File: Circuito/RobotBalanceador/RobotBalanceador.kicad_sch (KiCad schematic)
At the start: 57 parts, among them J1 Conn_01x04_Pin, J2 USB_B_Micro, J3 Barrel_Jack_Switch, J4 ENCODER, J5 ENCODER, J6 MOT 1, J7 MOT 2, SW1 SW_SPDT, U1 STM32F103C8Tx, U2 LMR62014XMF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

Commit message: Referencias y textos ajustados
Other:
- note added: "4) DRV8870 Datasheet"
- note removed: "4) L293D Shield"
- note removed: "4) L293x Ti"
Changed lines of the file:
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@@
 		)
 	)
-	(text "4) L293D Shield"
-		(exclude_from_sim no)
-		(at 12.446 182.626 0)
-		(effects
-			(font
-				(size 1.27 1.27)
-			)
-			(justify left bottom)
-			(href "http://wiki.sunfounder.cc/index.php?title=L293D_Motor_Driver_Shield")
+	(text "4) DRV8870 Datasheet"
+		(exclude_from_sim no)
+		(at 12.446 180.086 0)
+		(effects
+			(font
+				(size 1.27 1.27)
+			)
+			(justify left bottom)
+			(href "https://www.ti.com/lit/ds/symlink/drv8870.pdf")
 		)
 	)
@@
 	(text "5) MPU6050 Adafruit"
 		(exclude_from_sim no)
-		(at 12.446 186.436 0)
+		(at 12.446 183.642 0)
 		(effects
 			(font
@@
 		)
 	)
-	(text "4) L293x Ti"
-		(exclude_from_sim no)
-		(at 12.446 173.736 0)
-		(effects
-			(font
-				(size 1.27 1.27)
-			)
-			(justify left bottom)
-			(href "https://www.ti.com/lit/ds/symlink/l293.pdf")
-		)
-	)
 	(text "*C) Puede que no sea necesario el switch mejor\nquitar para reducir componentes"
 		(exclude_from_sim no)
@@
 	(text "6) Video de Phil 30:50"
 		(exclude_from_sim no)
-		(at 12.446 190.246 0)
-		(effects
-			(font
+		(at 12.446 187.452 0)
+		(effects
+			(font

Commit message: Secciones ajustadas
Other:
- note added: "2) Conv. Boost 3.7 ~ 5V & 12V"
- note added: "3) Regulación"
- note added: "4) Motores"
- note added: "5) IMU"
- note added: "7) Encoder"
- note removed: "2) Conv. Boost 3.7 LIPO a 12V (LMR62014)"
- note removed: "3) Regulación 5V a 3.3V"
- note removed: "4) Puente H (DRV8870DDA)"
- note removed: "5) IMU (MPU6050)"
- note removed: "6) Conector p/ encoder"
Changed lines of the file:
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@@
 		)
 	)
-	(text "6) Conector p/\nencoder\n"
+	(text "7) Encoder"
 		(exclude_from_sim no)
-		(at 245.11 123.19 0)
+		(at 244.602 118.872 0)
 		(effects
 			(font
@@
 		)
 	)
-	(text "3) Regulación 5V a 3.3V"
+	(text "3) Regulación"
 		(exclude_from_sim no)
-		(at 207.772 19.304 0)
+		(at 207.518 18.542 0)
 		(effects
 			(font
@@
 		)
 	)
-	(text "4) Puente H (DRV8870DDA)"
+	(text "4) Motores"
 		(exclude_from_sim no)
 		(at 115.062 106.426 0)
@@
 		)
 	)
-	(text "2) Conv. Boost 3.7 LIPO a 12V\n(LMR62014)"
+	(text "2) Conv. Boost 3.7 ~ 5V & 12V"
 		(exclude_from_sim no)
-		(at 115.062 22.86 0)
+		(at 115.062 19.05 0)
 		(effects
 			(font
@@
 		)
 	)
-	(text "5) IMU (MPU6050)"
+	(text "5) IMU"
 		(exclude_from_sim no)
 		(at 207.772 56.896 0)

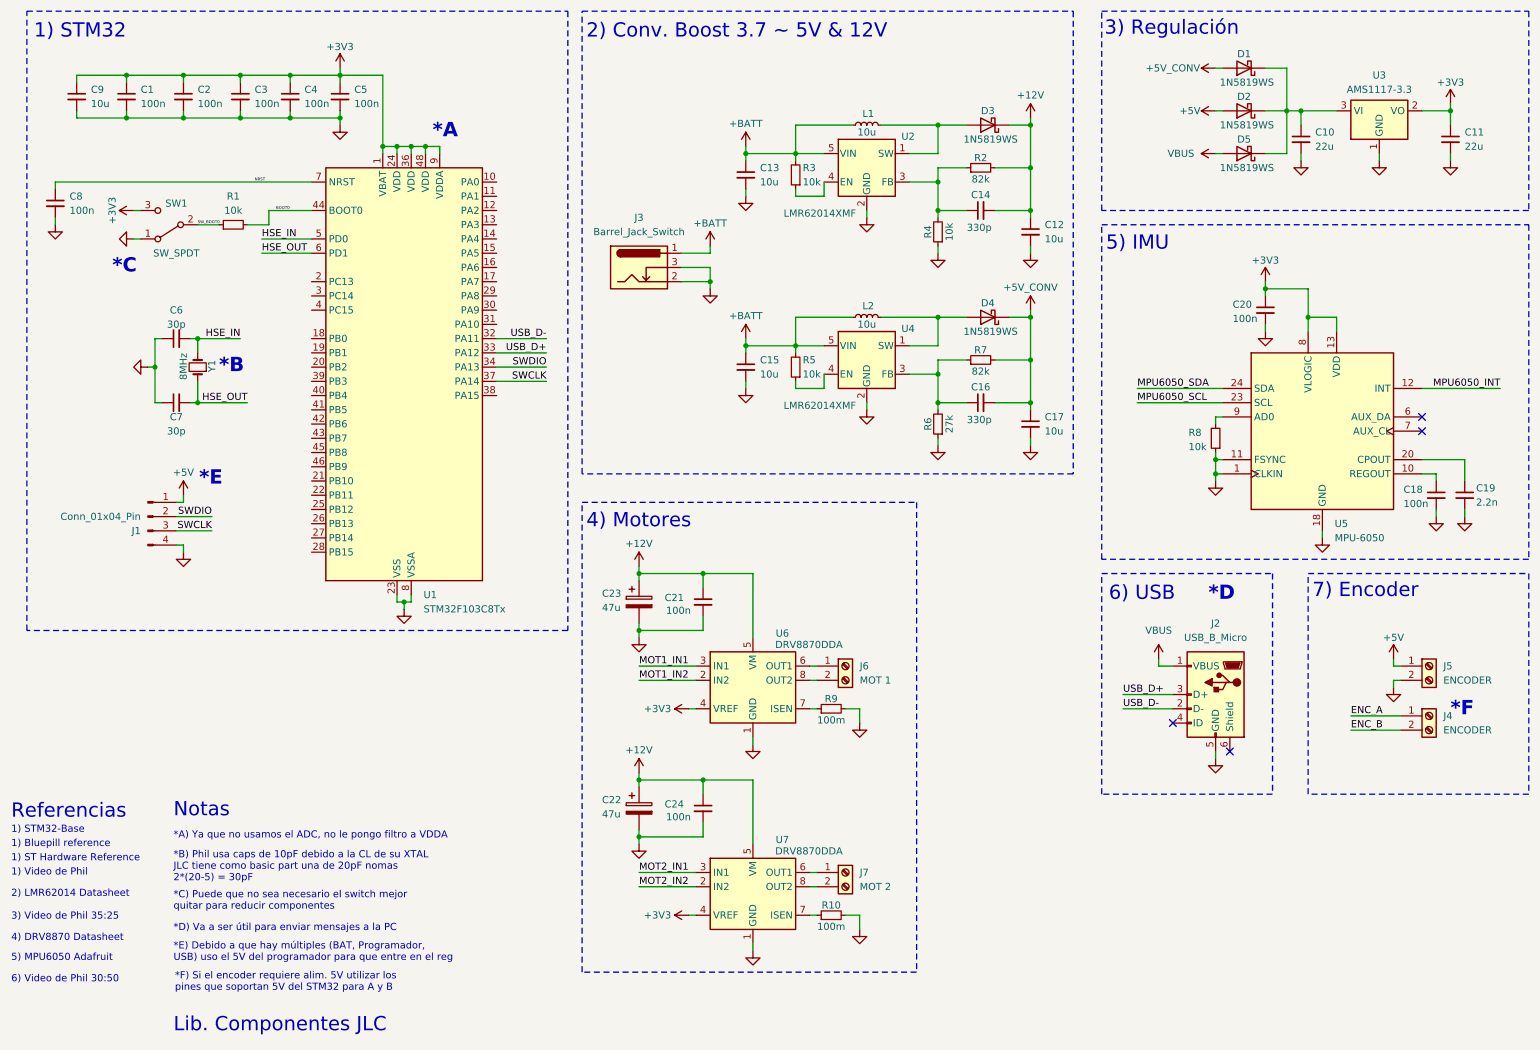
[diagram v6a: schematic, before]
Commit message: Añadido código/configuraciones para IMU y Encoder
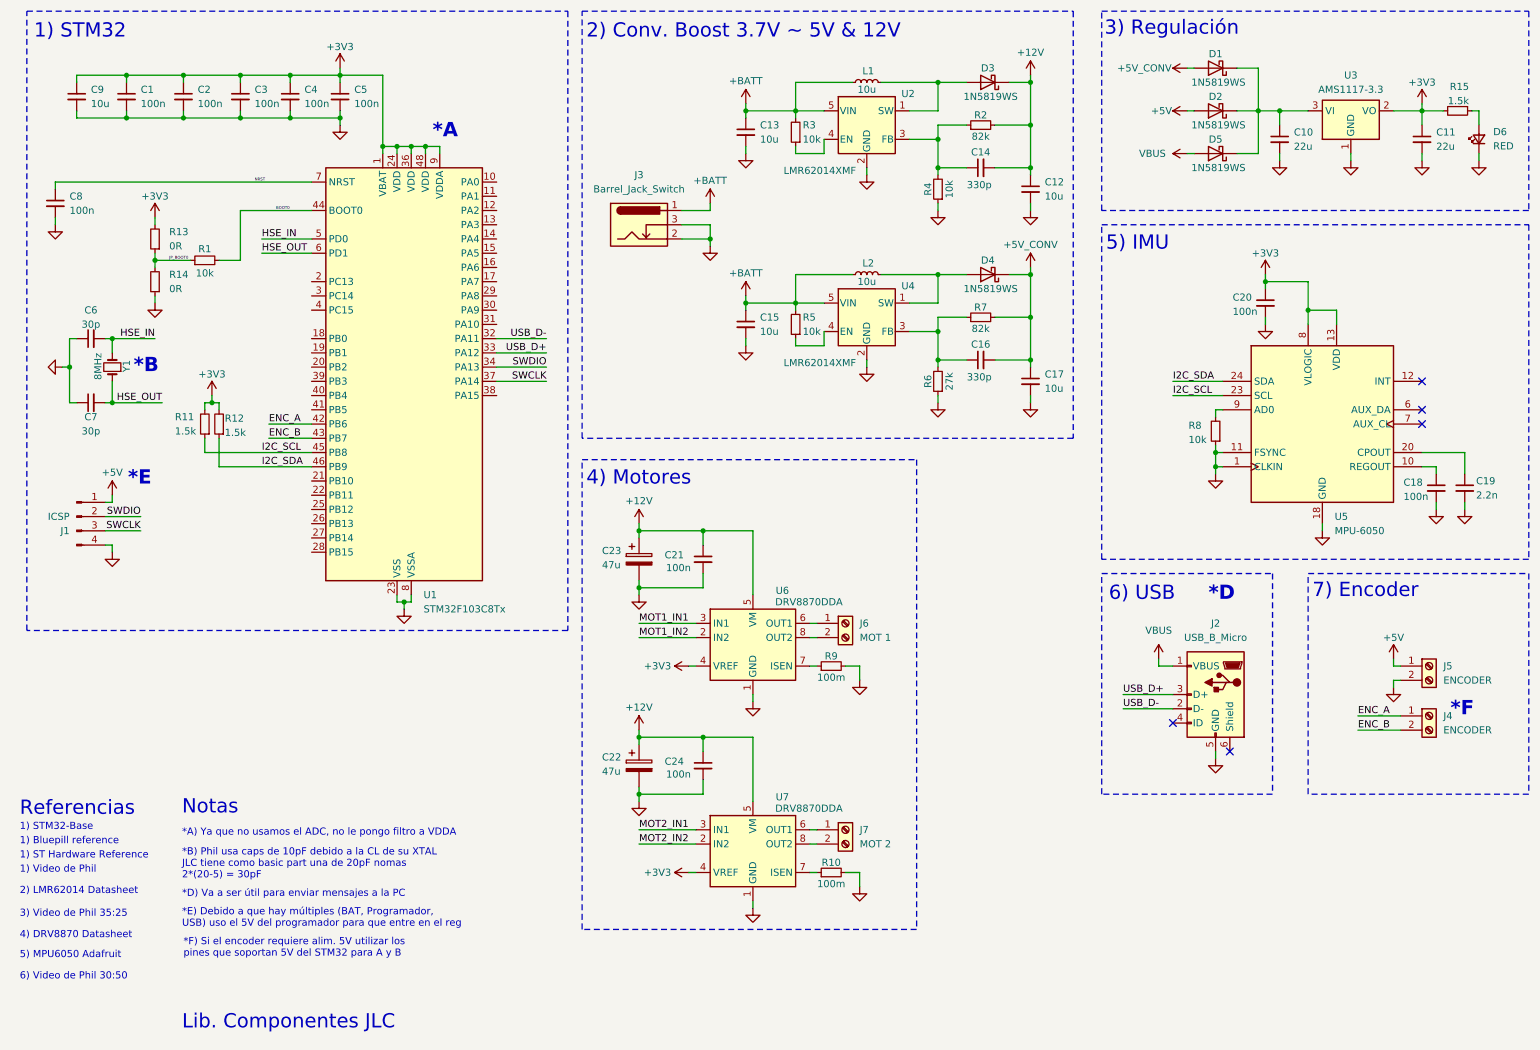
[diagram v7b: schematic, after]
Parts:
- removed SW1: SW_SPDT, symbol Switch:SW_SPDT
- added D6: RED, LED_SMD:LED_0603_1608Metric, symbol Device:LED_Small
- added R11, R12, R15: 1.5k, Resistor_SMD:R_0603_1608Metric, symbol Device:R_Small
- added R13, R14: 0R, Resistor_SMD:R_0402_1005Metric, symbol Device:R_Small
- J1: value Conn_01x04_Pin -> ICSP
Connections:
- net MPU6050_SCL is gone; now on net I2C_SCL: U5.23 (SCL)
- net MPU6050_SDA is gone; now on net I2C_SDA: U5.24 (SDA)
- net +3V3: now also R11.2, R12.2, R13.2, R15.2
- net ENC_A: now also U1.42 (PB6)
- net ENC_B: now also U1.43 (PB7)
- net GND: now also D6.1 (K), R14.1
- net I2C_SCL: now reaches U1.45 (PB8)
- net I2C_SCL: now also R11.1
- net I2C_SDA: now reaches U1.46 (PB9)
- net I2C_SDA: now also R12.1
- net MPU6050_INT: no longer names the net of U5.12 (INT)
- net SW_BOOT0 renamed JP_BOOT0
- net JP_BOOT0: now also R13.1, R14.2
- new net: D6.2 (A), R15.1
- no-connect marks 4 -> 5
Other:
- note added: "2) Conv. Boost 3.7V ~ 5V & 12V"
- note removed: "*C"
- note removed: "*C) Puede que no sea necesario el switch mejor quitar para reducir componentes"
- note removed: "2) Conv. Boost 3.7 ~ 5V & 12V"
- moved on the sheet: C10, C11, C12, C13, C14, C15, C16, C17, C18, C19, C20, C21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

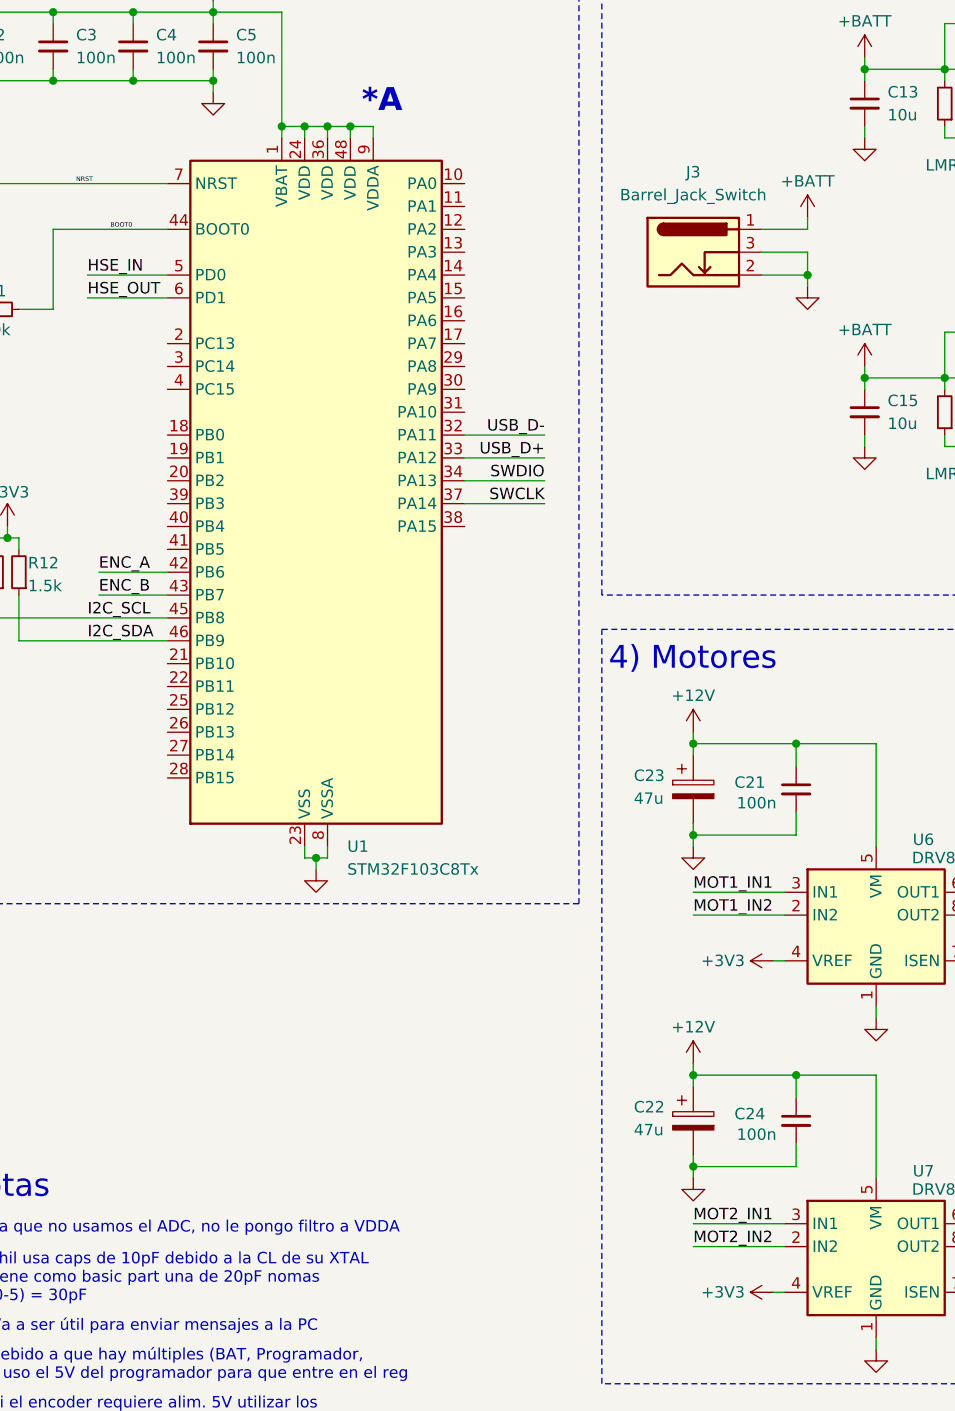
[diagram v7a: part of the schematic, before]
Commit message: Asignados pines p/ motores y TIM2 PWM @1kHz
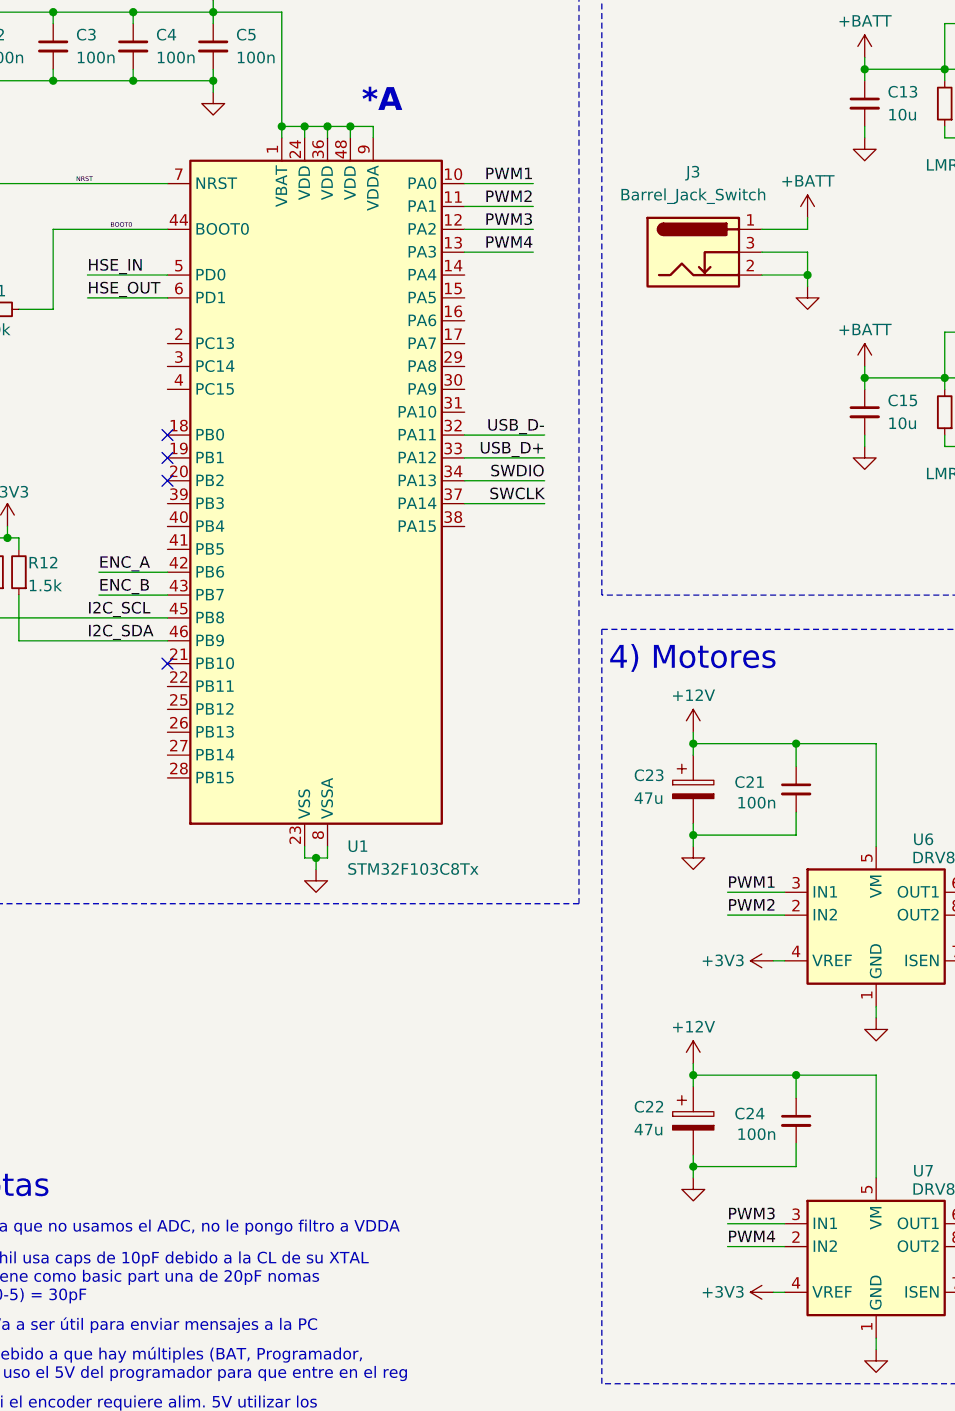
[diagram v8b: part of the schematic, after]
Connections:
- net MOT1_IN1 is gone; now on net PWM1: U6.3 (IN1)
- net MOT1_IN2 is gone; now on net PWM2: U6.2 (IN2)
- net MOT2_IN1 is gone; now on net PWM3: U7.3 (IN1)
- net MOT2_IN2 is gone; now on net PWM4: U7.2 (IN2)
- net PWM1: now reaches U1.10 (PA0)
- net PWM2: now reaches U1.11 (PA1)
- net PWM3: now reaches U1.12 (PA2)
- net PWM4: now reaches U1.13 (PA3)
- no-connect marks 5 -> 9
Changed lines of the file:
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@@
+	)
+	(no_connect
+		(at 66.04 97.79)
+	)
+	(no_connect
+		(at 66.04 74.93)
 	)
 	(no_connect
@@
 	)
 	(no_connect
+		(at 66.04 72.39)
+	)
+	(no_connect
+		(at 66.04 77.47)
+	)
+	(no_connect
 		(at 264.16 87.63)
 	)
@@
 	(wire
 		(pts
+			(xy 99.06 52.07) (xy 106.68 52.07)
+		)
+		(stroke
+			(width 0)
+			(type default)
+		)
+	)
+	(wire
+		(pts
 			(xy 57.15 57.15) (xy 66.04 57.15)
 		)
@@
 	(wire
 		(pts
+			(xy 99.06 46.99) (xy 106.68 46.99)
+		)
+		(stroke
+			(width 0)
+			(type default)
+		)
+	)
+	(wire
+		(pts
 			(xy 78.74 39.37) (xy 78.74 38.1)
 		)
@@
 	(wire
 		(pts
-			(xy 124.46 125.73) (xy 134.62 125.73)
+			(xy 128.27 125.73) (xy 134.62 125.73)
 		)
 		(stroke
@@
 	(wire
 		(pts
-			(xy 124.46 123.19) (xy 134.62 123.19)
-		)
-		(stroke
-			(width 0)
-			(type default)
-		)
-	)
-	(wire
-		(pts
-			(xy 124.46 160.02) (xy 134.62 160.02)
+			(xy 128.27 123.19) (xy 134.62 123.19)
+		)
+		(stroke
+			(width 0)
+			(type default)
+		)
+	)
+	(wire
+		(pts
+			(xy 128.27 160.02) (xy 134.62 160.02)
 		)
 		(stroke
@@
 	(wire
 		(pts
+			(xy 99.06 44.45) (xy 106.68 44.45)
+		)
+		(stroke
+			(width 0)
+			(type default)
+		)
+	)
+	(wire
+		(pts
 			(xy 143.51 72.39) (xy 143.51 73.66)
 		)
@@
 	(wire
 		(pts
-			(xy 124.46 162.56) (xy 134.62 162.56)
+			(xy 128.27 162.56) (xy 134.62 162.56)
 		)
 		(stroke
@@
 		(pts
 			(xy 187.96 68.58) (xy 194.31 68.58)
+		)
+		(stroke
+			(width 0)
+			(type default)
+		)
+	)
+	(wire
+		(pts
+			(xy 99.06 49.53) (xy 106.68 49.53)
 		)
 		(stroke
@@
 		)
 	)
-	(label "MOT2_IN1"
-		(at 124.46 160.02 0)
+	(label "PWM3"
+		(at 128.27 160.02 0)
 		(fields_autoplaced yes)
 		(effects
@@
 		)
 	)
-	(label "MOT1_IN2"
-		(at 124.46 125.73 0)
+	(label "PWM2"
+		(at 128.27 125.73 0)
 		(fields_autoplaced yes)
 		(effects
@@
 		)
 	)
-	(label "MOT1_IN1"
-		(at 124.46 123.19 0)
+	(label "PWM1"
+		(at 128.27 123.19 0)
 		(fields_autoplaced yes)
 		(effects
@@
 		)
 	)
-	(label "MOT2_IN2"
-		(at 124.46 162.56 0)
+	(label "PWM4"
+		(at 106.68 52.07 180)
+		(fields_autoplaced yes)
+		(effects
+			(font
+				(size 1.27 1.27)
+			)
+			(justify right bottom)
+		)
+	)
+	(label "PWM4"
+		(at 128.27 162.56 0)
 		(fields_autoplaced yes)
 		(effects
@@
 		)
 	)
+	(label "PWM3"
+		(at 106.68 49.53 180)
+		(fields_autoplaced yes)
+		(effects
+			(font
+				(size 1.27 1.27)
+			)
+			(justify right bottom)
+		)
+	)
 	(label "I2C_SCL"
 		(at 219.71 82.55 0)
@@
 		)
 	)
+	(label "PWM2"
+		(at 106.68 46.99 180)
+		(fields_autoplaced yes)
+		(effects
+			(font
+				(size 1.27 1.27)
+			)
+			(justify right bottom)
+		)
+	)
 	(label "HSE_IN"
 		(at 38.1 72.39 180)
@@
 		)
 	)
+	(label "PWM1"
+		(at 106.68 44.45 180)
+		(fields_autoplaced yes)
+		(effects
+			(font
+				(size 1.27 1.27)
+			)
+			(justify right bottom)
+		)
+	)
